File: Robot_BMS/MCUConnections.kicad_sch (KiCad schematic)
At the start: 1 part, among them J2 Conn_01x14_Pin

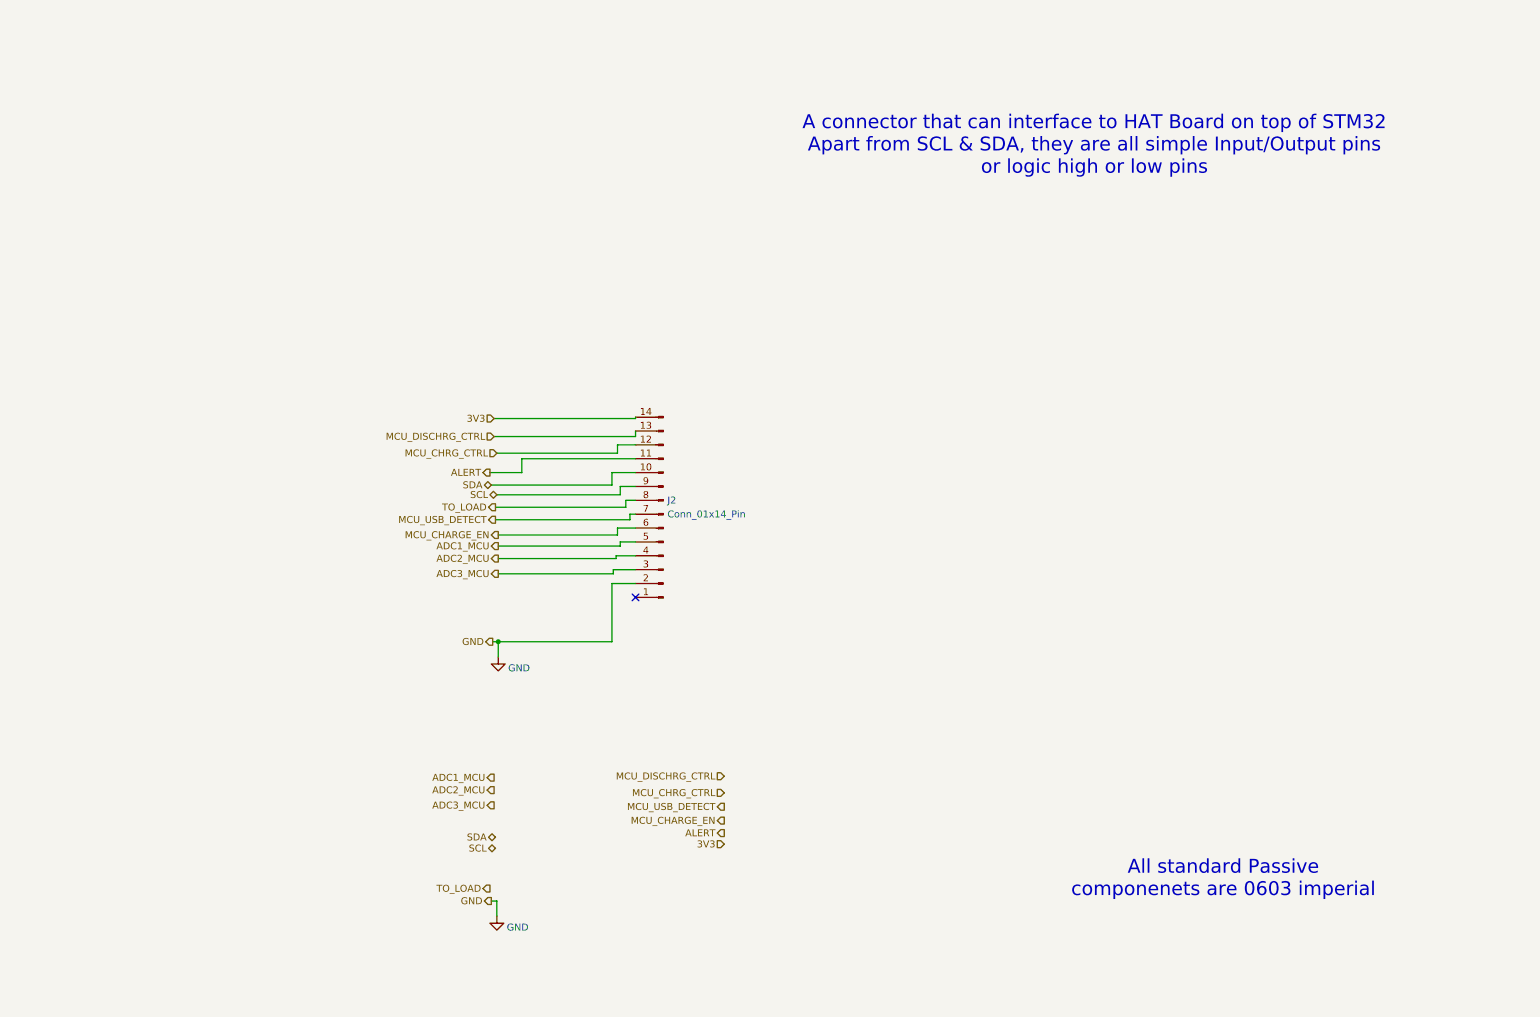
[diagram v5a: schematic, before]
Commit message: placed connectors for BMS PCB
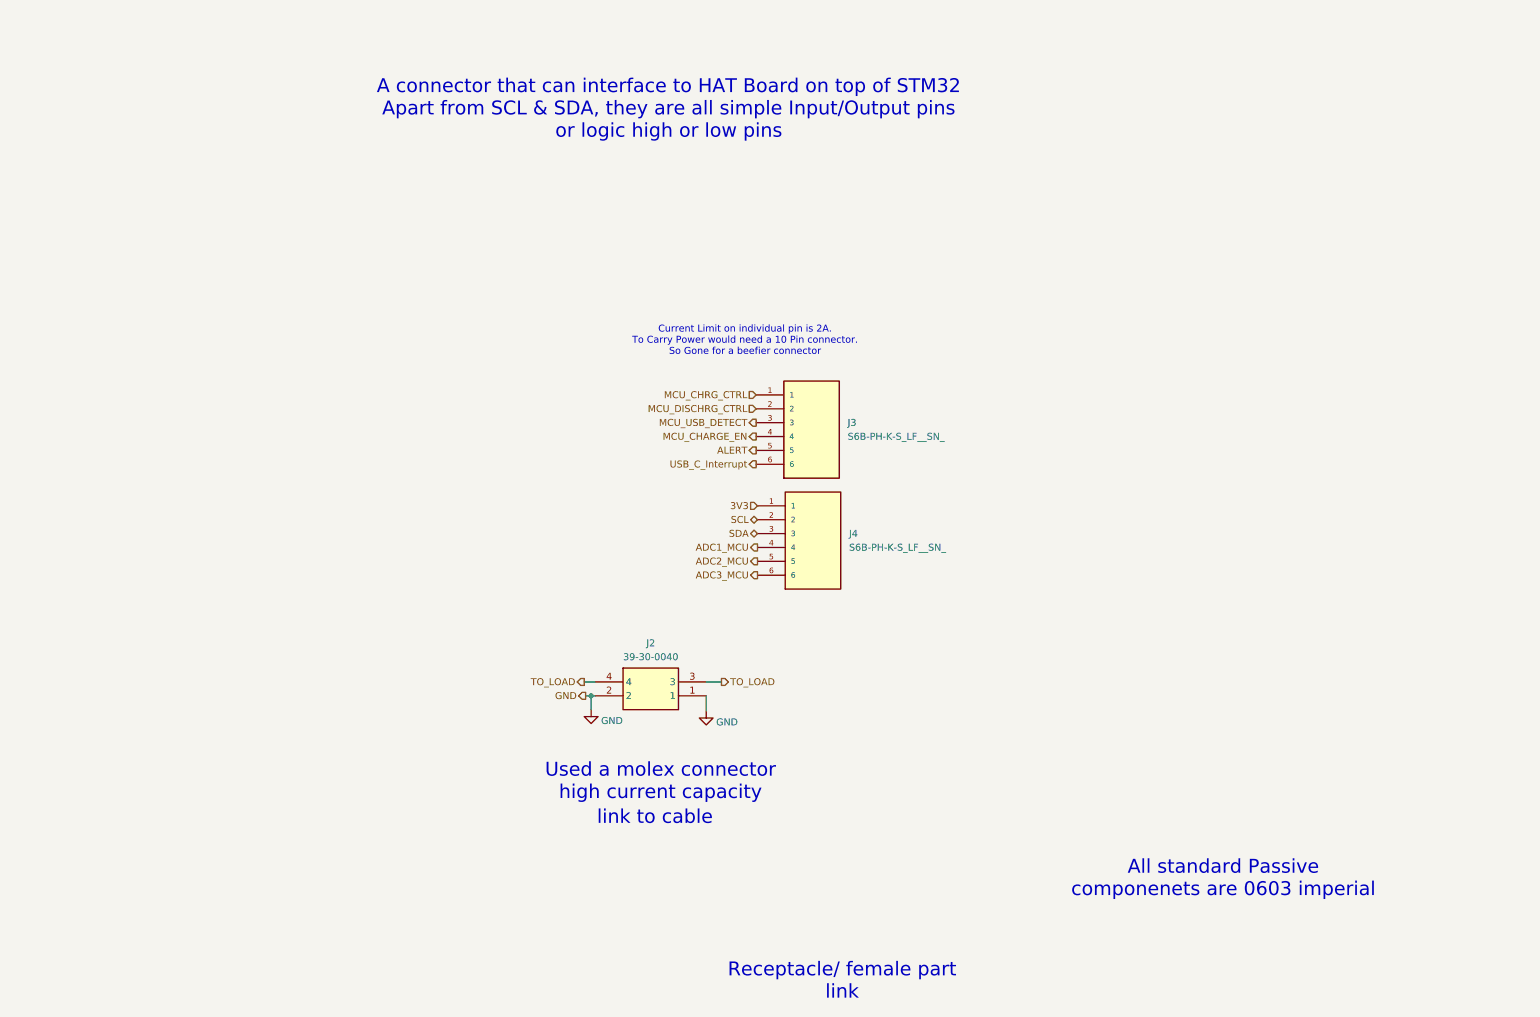
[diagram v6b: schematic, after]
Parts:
- removed J2: Conn_01x14_Pin, Connector_PinHeader_2.54mm:PinHeader_1x14_P2.54mm_Vertical, symbol Connector:Conn_01x14_Pin
- added J2: 39-30-0040, RobotBMS:39-30-Y040, symbol 39-30-0040:39-30-0040
- added J3, J4: S6B-PH-K-S_LF__SN_, RobotBMS:JST_S6B-PH-K-S_LF__SN_, symbol S6B-PH-K-S_LF__SN_:S6B-PH-K-S_LF__SN_
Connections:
- net 3V3: now also J4.1
- net ADC1_MCU: now also J4.4
- net ADC2_MCU: now also J4.5
- net ADC3_MCU: now also J4.6
- net ALERT: now also J3.5
- net GND: now also J2.1, J2.2
- net MCU_CHARGE_EN: now also J3.4
- net MCU_CHRG_CTRL: now also J3.1
- net MCU_DISCHRG_CTRL: now also J3.2
- net MCU_USB_DETECT: now also J3.3
- net SCL: now also J4.2
- net SDA: now also J4.3
- net TO_LOAD: now also J2.3, J2.4
- new net USB_C_Interrupt: J3.6
- no-connect marks 1 -> 0
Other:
- note added: "Current Limit on individual pin is 2A. To Carry Power would need a 10 Pin connector. So Gone for a beefier connector"
- note added: "Receptacle/ female part link"
- note added: "Used a molex connector high current capacity"
- note added: "link to cable"

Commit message: adding qwik connectors replacing old jst ph 6 pin ones
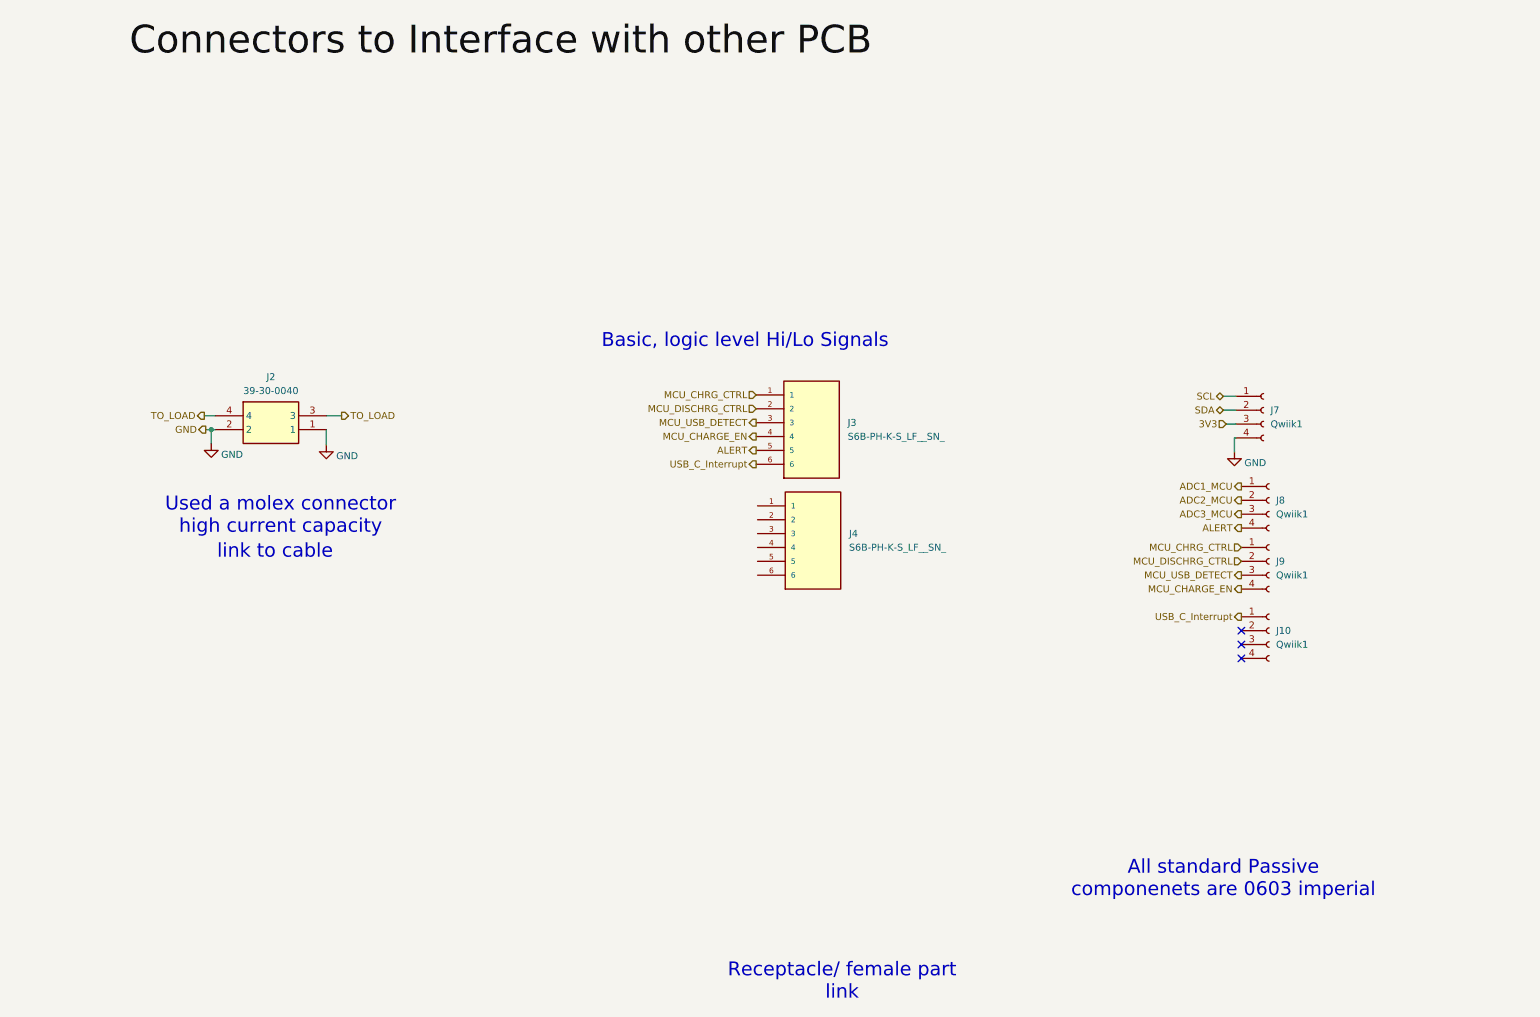
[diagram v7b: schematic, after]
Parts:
- added J10, J7, J8, J9: Qwiik1, Connector_JST:JST_SH_BM04B-SRSS-TB_1x04-1MP_P1.00mm_Vertical, symbol Connector:Conn_01x04_Socket
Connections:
- net 3V3: now also J7.3 (Pin_3); no longer J4.1
- net ADC1_MCU: now also J8.1 (Pin_1); no longer J4.4
- net ADC2_MCU: now also J8.2 (Pin_2); no longer J4.5
- net ADC3_MCU: now also J8.3 (Pin_3); no longer J4.6
- net ALERT: now also J8.4 (Pin_4)
- net GND: now also J7.4 (Pin_4)
- net MCU_CHARGE_EN: now also J9.4 (Pin_4)
- net MCU_CHRG_CTRL: now also J9.1 (Pin_1)
- net MCU_DISCHRG_CTRL: now also J9.2 (Pin_2)
- net MCU_USB_DETECT: now also J9.3 (Pin_3)
- net SCL: now also J7.1 (Pin_1); no longer J4.2
- net SDA: now also J7.2 (Pin_2); no longer J4.3
- net USB_C_Interrupt: now also J10.1 (Pin_1)
- no-connect marks 0 -> 3
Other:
- note added: "Basic, logic level Hi/Lo Signals"
- note removed: "A connector that can interface to HAT Board on top of STM32 Apart from SCL & SDA, they are all simple Input/Output pins or logic high or low pins"
- note removed: "Current Limit on individual pin is 2A. To Carry Power would need a 10 Pin connector. So Gone for a beefier connector"
- moved on the sheet: J2

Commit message: qwikk connector 3d model and footprint in RobotBMS
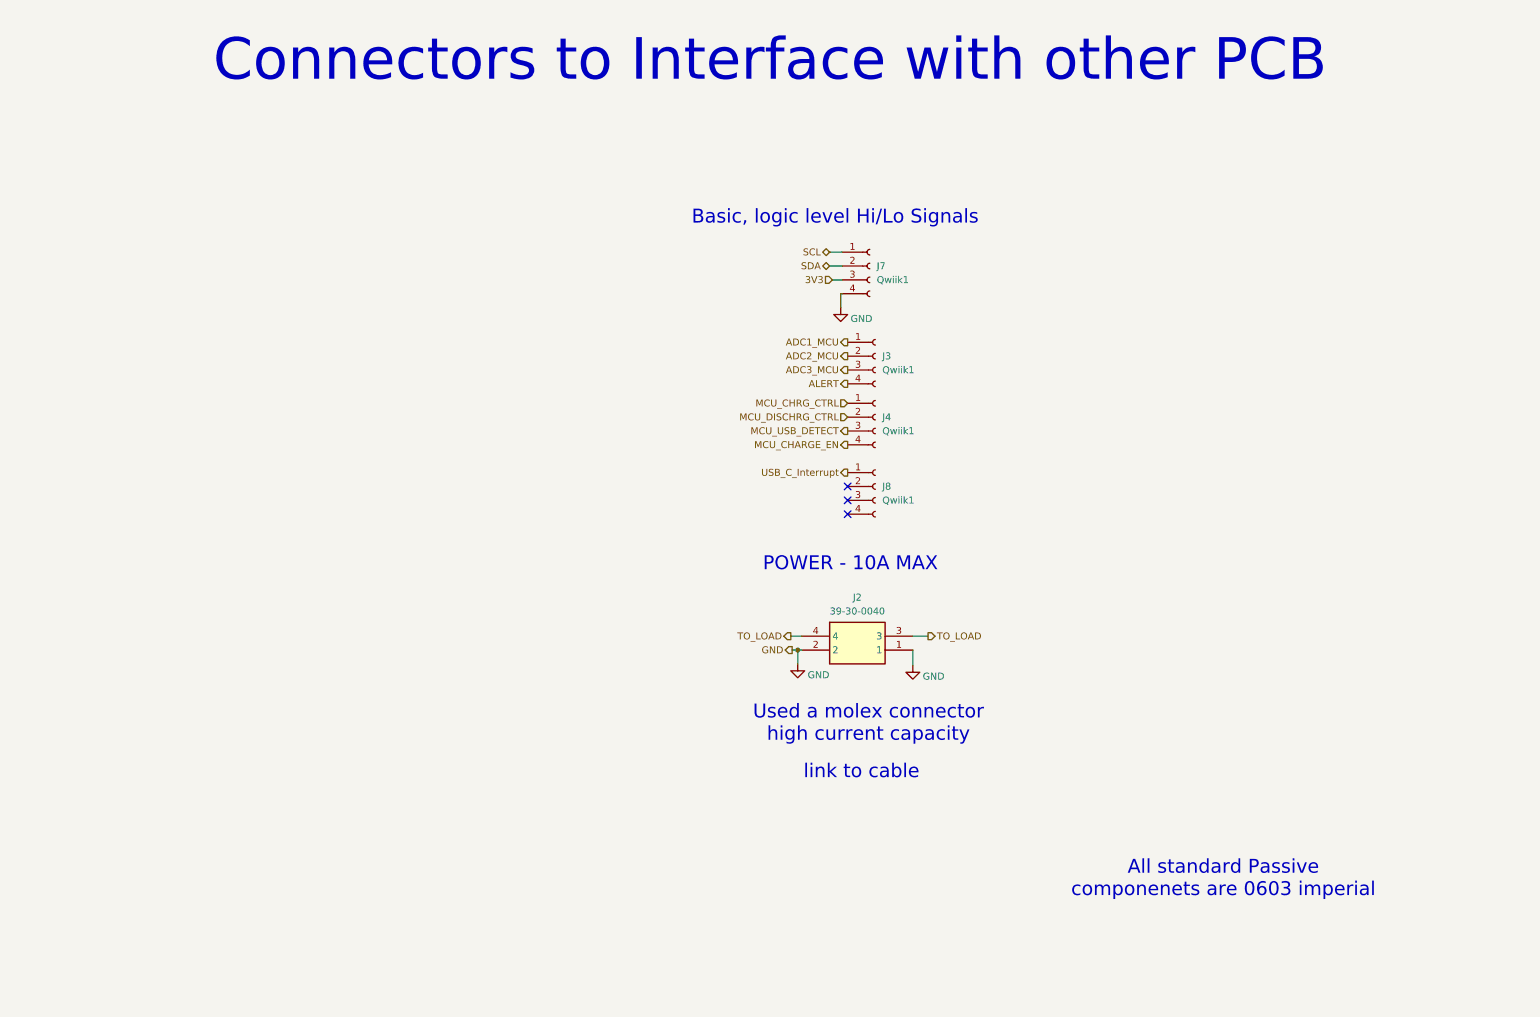
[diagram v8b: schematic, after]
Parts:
- removed J10, J9: Qwiik1, Connector_JST:JST_SH_BM04B-SRSS-TB_1x04-1MP_P1.00mm_Vertical, symbol Connector:Conn_01x04_Socket
- removed J3, J4: S6B-PH-K-S_LF__SN_, RobotBMS:JST_S6B-PH-K-S_LF__SN_, symbol S6B-PH-K-S_LF__SN_:S6B-PH-K-S_LF__SN_
- added J3, J4: Qwiik1, RobotBMS:JST_SH_BM04B-SRSS-TB_1x04-1MP_P1.00mm_Vertical, symbol Connector:Conn_01x04_Socket
- J7, J8: footprint Connector_JST:JST_SH_BM04B-SRSS-TB_1x04-1MP_P1.00mm_Vertical -> RobotBMS:JST_SH_BM04B-SRSS-TB_1x04-1MP_P1.00mm_Vertical; Manufacturer_Part_Number (none) -> SM04B-SRSS-TB(LFSN); Price (none) -> 0.42
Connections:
- net ADC1_MCU: now also J3.1 (Pin_1); no longer J8.1 (Pin_1)
- net ADC2_MCU: now also J3.2 (Pin_2); no longer J8.2 (Pin_2)
- net ADC3_MCU: now also J3.3 (Pin_3); no longer J8.3 (Pin_3)
- net ALERT: now also J3.4 (Pin_4); no longer J8.4 (Pin_4)
- net MCU_CHARGE_EN: now also J4.4 (Pin_4)
- net MCU_CHRG_CTRL: now also J4.1 (Pin_1)
- net MCU_DISCHRG_CTRL: now also J4.2 (Pin_2)
- net MCU_USB_DETECT: now also J4.3 (Pin_3)
- net USB_C_Interrupt: now also J8.1 (Pin_1)
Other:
- note added: "Connectors to Interface with other PCB"
- note added: "POWER - 10A MAX"
- note removed: "Receptacle/ female part link"
- moved on the sheet: J2, J7
